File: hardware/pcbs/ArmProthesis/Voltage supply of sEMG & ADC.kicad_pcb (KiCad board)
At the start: 4 copper layers, 50.2 x 51.8 mm, 64 parts, among them Q1 BC817, Q2 BC817, Q3 BC817, U1 LT3045xMSE, U2 TPS7A4701RGWR, U3 LT8471EFE_TRPBF, U4 LT3094xMSE

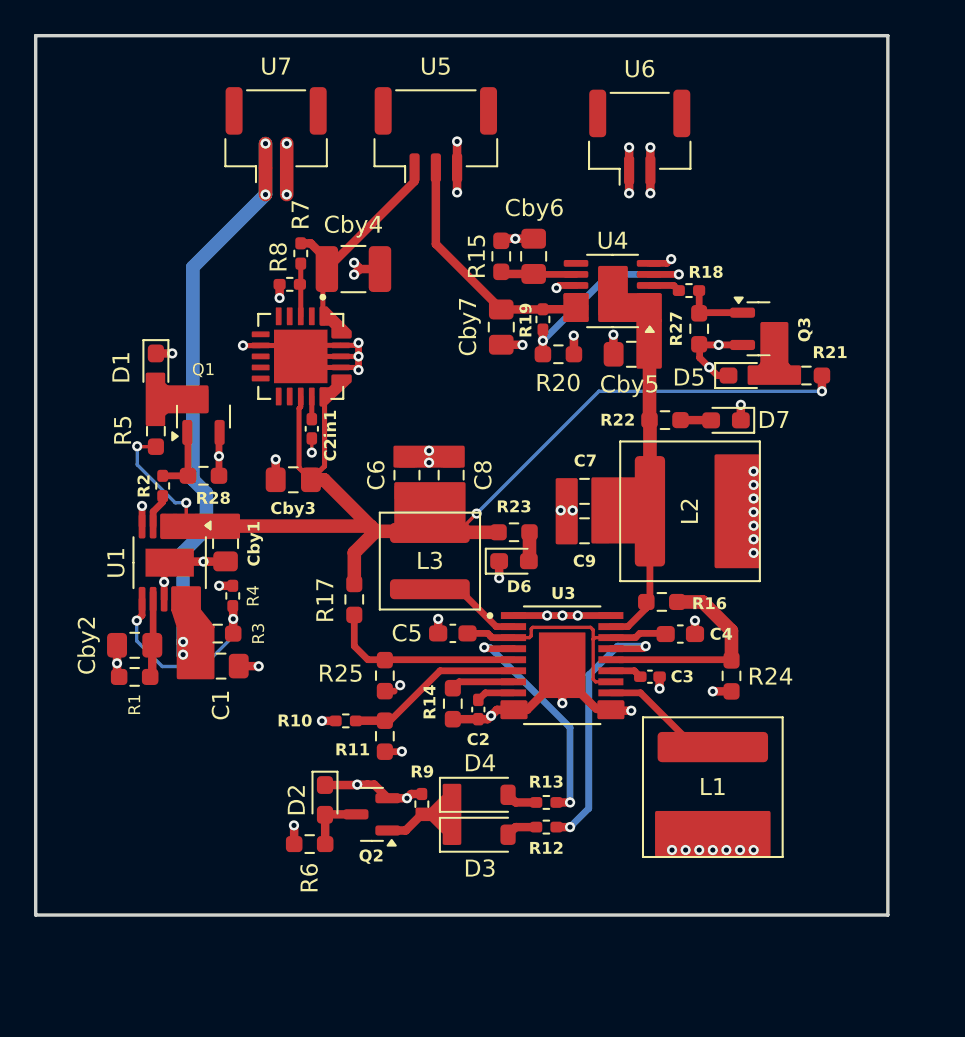
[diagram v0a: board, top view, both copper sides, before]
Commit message: Fixes
sEMG - minor
Voltage supply... - major but not fixed
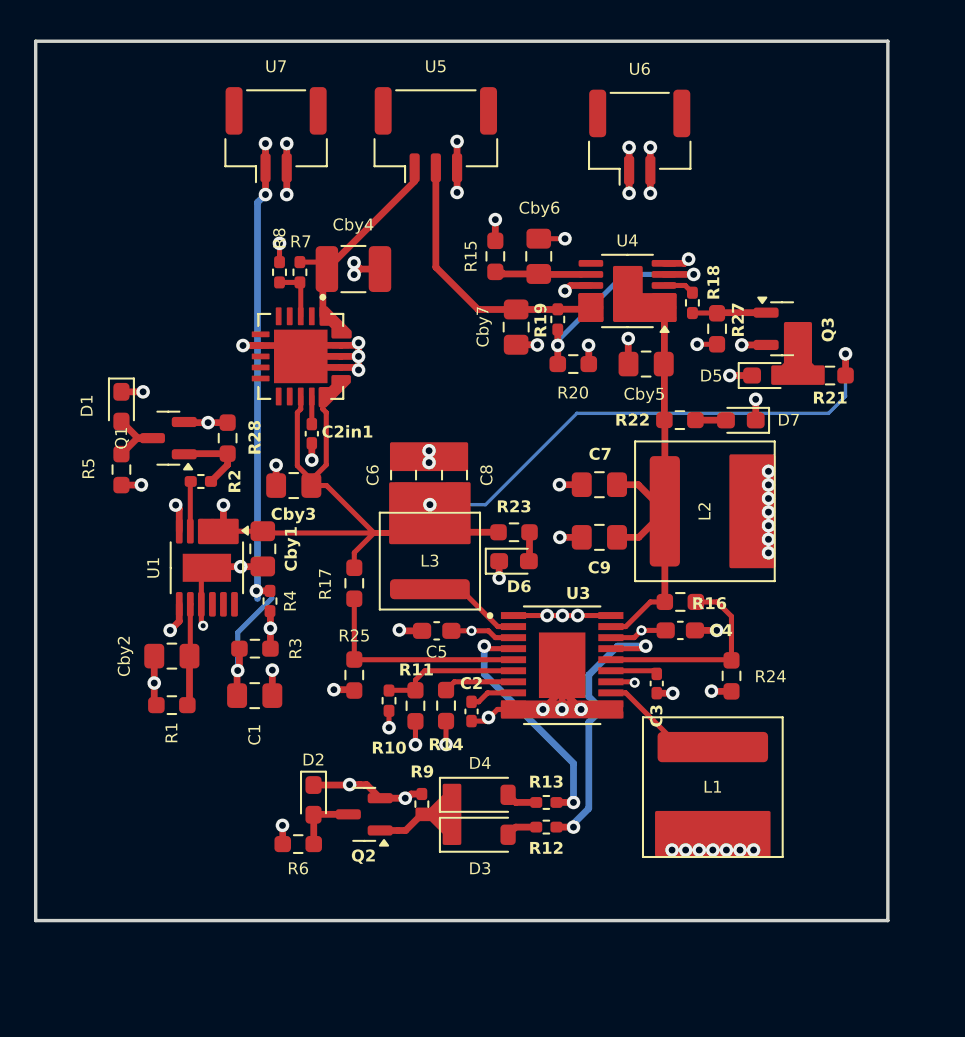
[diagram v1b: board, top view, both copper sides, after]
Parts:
- moved D1 3.04 mm to (99.2, 64.2)
- moved R5 3.04 mm to (99.2, 67.9)
- moved R10 2.81 mm to (114.9, 81.5), turned to -90 degrees
- moved R1 2.75 mm to (102.2, 81.8)
- moved C1 2.63 mm to (107.0, 81.2)
- moved R28 2.63 mm to (105.4, 66.1), turned to 90 degrees
- moved R11 2.54 mm to (116.5, 81.8)
- moved Q1 2.43 mm to (102.0, 66.1), turned to 180 degrees
- moved R3 2.36 mm to (107.1, 78.5)
- moved Cby2 2.28 mm to (102.2, 78.9)
- moved R2 2.26 mm to (103.9, 68.6), turned to 0 degrees
- moved Cby1 2.21 mm to (107.5, 72.6)
- moved R4 2.21 mm to (107.9, 75.6)
- moved U1 2.21 mm to (104.2, 73.7)
- moved R25 1.80 mm to (112.9, 80.0)
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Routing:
- net /+11.1V: track 112.7 -> 10.5 mm
- net GND: track 86.1 -> 99.0 mm, vias 55 -> 59
- net -6V: track 17.5 -> 27.3 mm
- net Net-(U3-SHOUT): track 16.6 -> 23.0 mm, vias 0 -> 3
- net +6V: track 67.9 -> 74.2 mm
- net Net-(D1-A): track 0.00 -> 4.44 mm
- net /+5V: track 37.7 -> 34.9 mm, vias 4 -> 3
- net Net-(U3-OV/UV): track 10.5 -> 8.29 mm
- net Net-(U1-SET): track 4.33 -> 6.06 mm
- net /-5.5V: track 14.1 -> 15.8 mm
- net Net-(U1-PGFB): track 12.0 -> 10.5 mm
- net Net-(U3-FB1): track 11.5 -> 13.0 mm
- net Net-(U1-PG): track 2.00 -> 2.94 mm
- net Net-(U3-SS2): track 1.88 -> 2.78 mm
- net Net-(U3-FB2): track 12.2 -> 11.7 mm
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- added copper zone on In2.Cu, net /+11.1V
- added copper zone on F.Cu, net GND

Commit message: Additional to last push
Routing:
- net GND: vias 59 -> 58
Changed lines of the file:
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@@
-	)
-	(via
-		(at 117.3 67.5)
-		(size 0.8)
-		(drill 0.4)
-		(layers "F.Cu" "B.Cu")
-		(net 1)
 	)
 	(via
@@
 	)
 	(via
-		(at 117.3 66.8)
+		(at 117.3 67.15)
 		(size 0.8)
 		(drill 0.4)
@@
 	)
 	(segment
-		(start 101.6675 68.3575)
-		(end 98.5 68.3575)
-		(width 0.4)
+		(start 100.37125 68.810385)
+		(end 104.010385 68.810385)
+		(width 0.3)
 		(layer "In2.Cu")
 		(net 8)
 	)
 	(segment
-		(start 103.01 69.7)
-		(end 101.6675 68.3575)
-		(width 0.4)
+		(start 104.010385 68.810385)
+		(end 105.2 70)
+		(width 0.3)
 		(layer "In2.Cu")
 		(net 8)

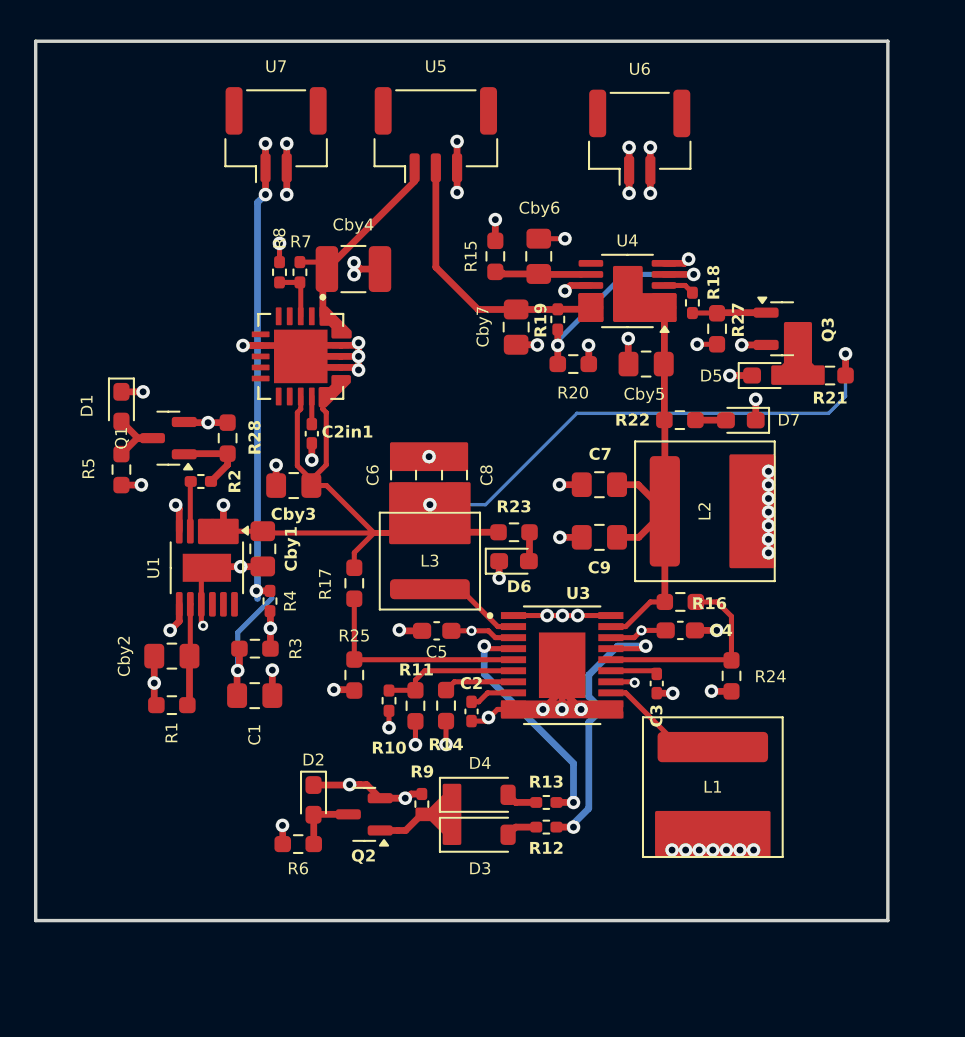
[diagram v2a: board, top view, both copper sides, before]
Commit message: Voltage supply sEMG & ADC v0.2
Major fixes. Mounting holes missing
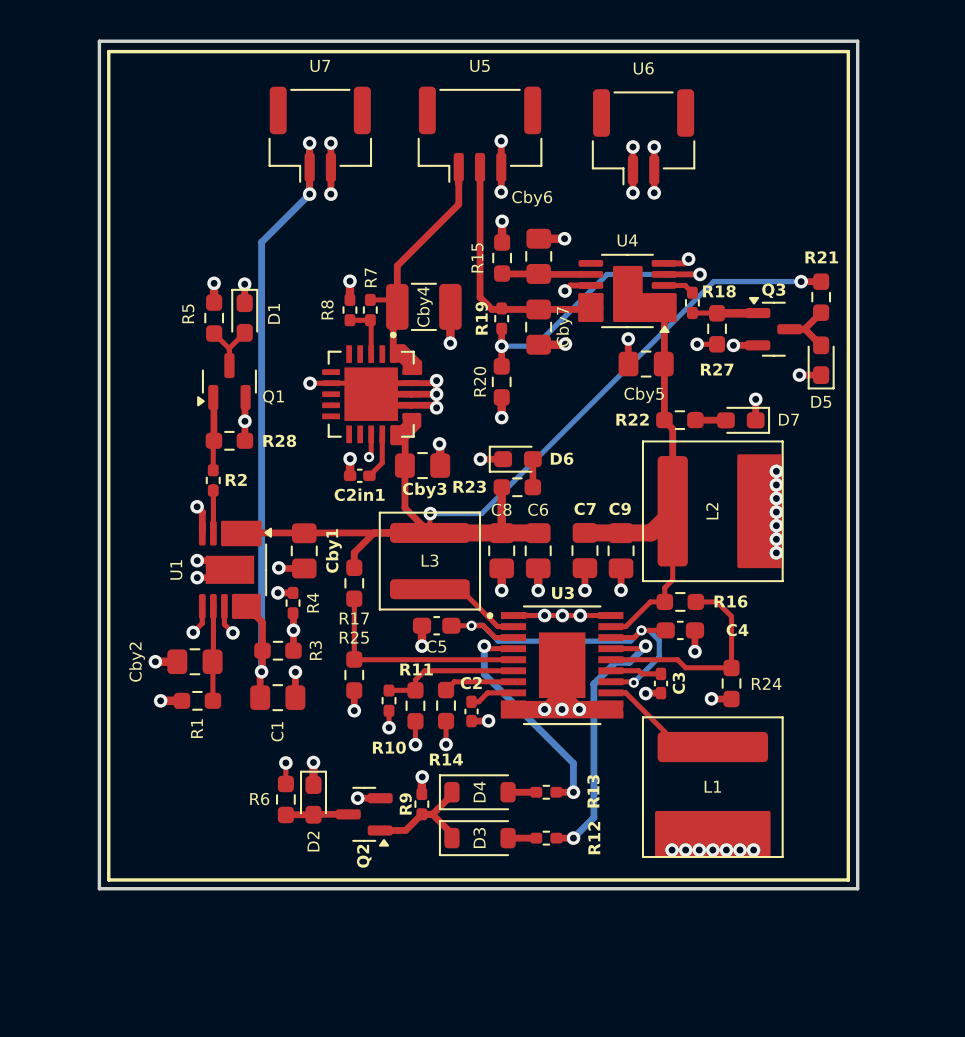
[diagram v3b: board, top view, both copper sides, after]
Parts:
- moved R5 10.5 mm to (104.7, 59.0), turned to 90 degrees
- moved C6 9.09 mm to (123.7, 72.7), turned to -90 degrees
- moved D1 8.94 mm to (106.5, 59.0)
- moved Cby3 7.67 mm to (116.9, 67.7), turned to 0 degrees
- moved D6 6.00 mm to (122.5, 67.3)
- moved C8 5.24 mm to (121.6, 72.7), turned to -90 degrees
- moved Q1 4.90 mm to (105.6, 62.7), turned to 90 degrees
- moved Cby4 4.70 mm to (117.0, 58.3)
- moved R7 4.70 mm to (113.8, 58.5)
- moved R8 4.70 mm to (112.6, 58.5)
- moved U2 4.70 mm to (113.9, 63.5)
- moved R21 4.64 mm to (140.4, 57.8), turned to 90 degrees
- moved R20 4.34 mm to (121.6, 62.8), turned to -90 degrees
- moved C7 3.97 mm to (126.5, 72.7), turned to 90 degrees
- moved C2in1 3.75 mm to (113.2, 68.3), turned to 180 degrees
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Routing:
- net +6V: track 74.5 -> 94.6 mm
- net GND: track 99.0 -> 91.7 mm, vias 58 -> 62
- net /+5V: track 34.9 -> 41.1 mm
- net Net-(D5-A): track 0.02 -> 4.52 mm
- net Net-(U4-PGFB): track 13.4 -> 17.4 mm
- net /+5.5V: track 14.2 -> 16.8 mm
- net Net-(D3-K): track 9.72 -> 7.69 mm
- net /-5.5V: track 15.8 -> 14.5 mm
- net Net-(U3-FB2): track 11.7 -> 12.8 mm
- net Net-(U2-NR): track 1.62 -> 2.75 mm
- net Net-(U3-SHOUT): track 23.0 -> 23.9 mm
- net Net-(Q3-B): track 4.36 -> 3.58 mm
- net -6V: track 27.3 -> 26.5 mm
- net Net-(D1-A): track 4.44 -> 3.76 mm
- net Net-(U1-SET): track 6.06 -> 5.44 mm
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- removed copper zone on F.Cu, net GND
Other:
- board size 50.2 x 51.8 mm -> 44.6 x 49.9 mm

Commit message: BMS v0.2v + polishment of Vsupply  board
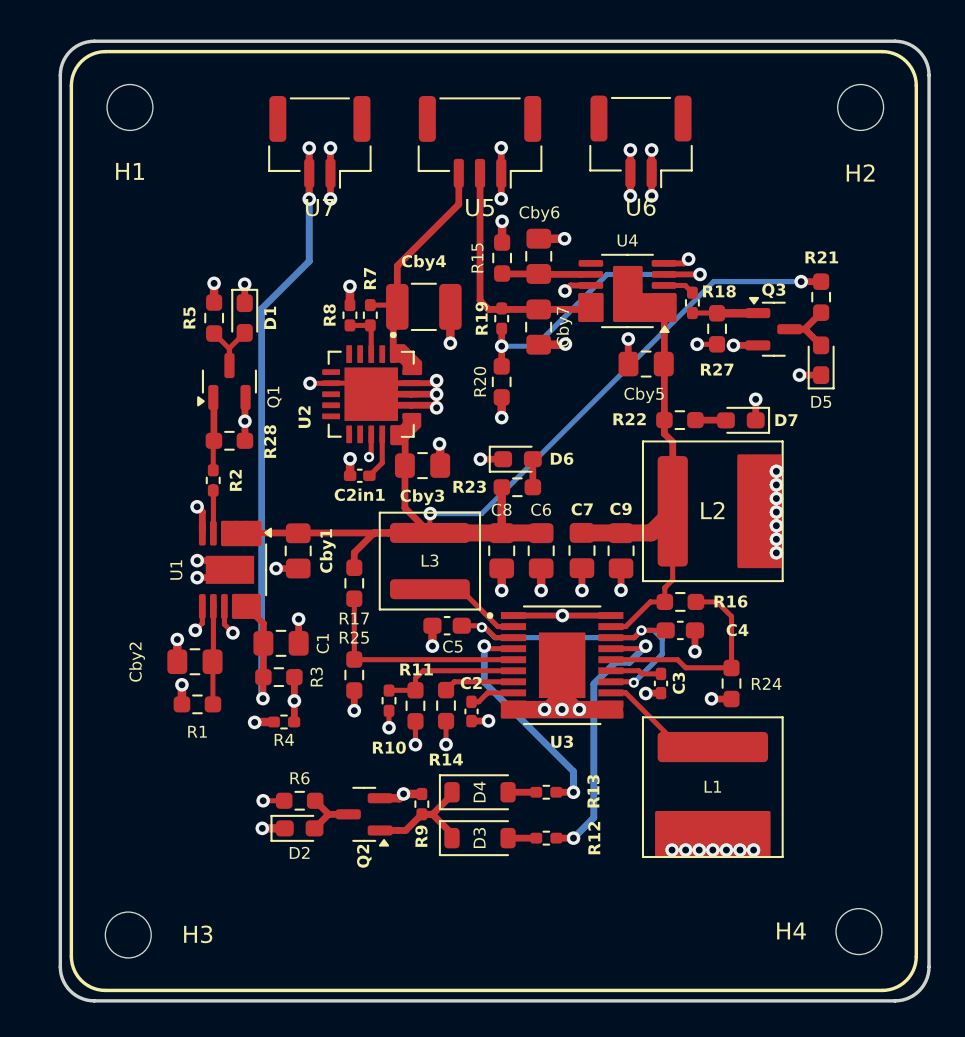
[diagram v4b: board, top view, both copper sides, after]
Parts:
- added H1: MountingHole, MountingHole:MountingHole_2.7mm_M2.5_DIN965, F.Cu at (99.7, 46.6)
- added H2: MountingHole, MountingHole:MountingHole_2.7mm_M2.5_DIN965, F.Cu at (142.7, 46.6)
- added H3: MountingHole, MountingHole:MountingHole_2.7mm_M2.5_DIN965, F.Cu at (99.6, 95.3)
- added H4: MountingHole, MountingHole:MountingHole_2.7mm_M2.5_DIN965, F.Cu at (142.6, 95.1)
- U5: footprint Connector_JST:JST_GH_BM03B-GHS-TBT_1x03-1MP_P1.25mm_Vertical -> Connector_JST:JST_GH_SM03B-GHS-TB_1x03-1MP_P1.25mm_Horizontal
- U6, U7: footprint Connector_JST:JST_GH_BM02B-GHS-TBT_1x02-1MP_P1.25mm_Vertical -> Connector_JST:JST_GH_SM02B-GHS-TB_1x02-1MP_P1.25mm_Horizontal
- moved R4 7.02 mm to (108.8, 82.8), turned to 0 degrees
- moved C1 3.20 mm to (108.6, 78.1)
- moved D2 1.86 mm to (109.7, 89.0), turned to 0 degrees
- moved R3 1.56 mm to (108.5, 80.1)
- moved R6 0.82 mm to (109.7, 87.4), turned to 180 degrees
- moved C5 0.61 mm to (118.4, 77.1)
- moved U7 0.45 mm to (110.9, 48.6), turned to 180 degrees
- moved U5 0.45 mm to (120.3, 48.6), turned to 180 degrees
- moved Cby1 0.36 mm to (109.6, 72.7)
- moved U6 0.31 mm to (129.8, 48.6), turned to 180 degrees
- moved R7 0.30 mm to (113.8, 58.8)
- moved R8 0.30 mm to (112.6, 58.8)
- moved R1 0.21 mm to (103.7, 81.7)
- moved C6 0.18 mm to (123.9, 72.7)
- moved C7 0.17 mm to (126.3, 72.7)
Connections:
- U5 pad 1: /+5.5V -> GND
- U5 pad 3: GND -> /+5.5V
- U7 pad 1: /+5V -> GND
- U7 pad 2: GND -> /+5V
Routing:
- net Net-(U1-PGFB): track 10.2 -> 12.2 mm
- net /+5V: track 41.1 -> 42.4 mm
- net Net-(U3-SHOUT): track 23.9 -> 22.7 mm
- net /+5.5V: track 16.8 -> 15.9 mm
- net GND: track 91.7 -> 91.9 mm, vias 62 -> 61
- net /+11.1V: vias 14 -> 12
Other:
- board size 44.6 x 49.9 mm -> 51.1 x 56.5 mm

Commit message: BMS v0.3 + main folder reconstruction
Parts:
- added G***: LOGO, LOGO, B.Cu at (105.4, 89.1)
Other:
- board text added: "SL-sEMG/ADC-PSU v0.3"

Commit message: Cosmetics xd
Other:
- board text added: "SL-sEMG&ADC-PSU v0.3"
- board text removed: "SL-sEMG/ADC-PSU v0.3"
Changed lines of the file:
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@@
 		(tags "connector JST GH horizontal")
 		(property "Reference" "U7"
-			(at 0 -3.9 180)
+			(at 0.025 -4.55 180)
 			(layer "F.SilkS")
 			(effects
@@
 		(tags "capacitor handsolder")
 		(property "Reference" "Cby7"
-			(at -0.025 -1.45 90)
+			(at 2.45 -0.025 180)
 			(layer "F.SilkS")
 			(effects
@@
 		(tags "connector JST GH horizontal")
 		(property "Reference" "U6"
-			(at 0 -3.9 180)
+			(at 0.025 -4.35 180)
 			(layer "F.SilkS")
 			(effects
@@
 		(tags "capacitor handsolder")
 		(property "Reference" "Cby2"
-			(at 3.465 0 90)
+			(at 2.6725 0.02 90)
 			(layer "F.SilkS")
 			(effects
@@
 		(tags "capacitor handsolder")
 		(property "Reference" "C4"
-			(at -3.3625 -0.009375 0)
+			(at -2.5625 0.025 0)
 			(layer "F.SilkS")
 			(effects
@@
 		(tags "connector JST GH horizontal")
 		(property "Reference" "U5"
-			(at 0 -3.9 180)
+			(at 0.175 0 180)
 			(layer "F.SilkS")
 			(effects
@@
 		)
 	)
-	(gr_text "SL-sEMG/ADC-PSU v0.3"
-		(at 132.85 46.85 0)
+	(gr_text "SL-sEMG&ADC-PSU v0.3"
+		(at 135.35 46.6 0)
 		(layer "B.SilkS")
 		(effects

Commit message: Vs of sEMG and ADC v0.4
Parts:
- moved R24 5.22 mm to (136.8, 75.6), turned to 0 degrees
- moved C7 3.31 mm to (127.5, 69.6), turned to 0 degrees
- moved R25 2.80 mm to (112.9, 77.2)
- moved R17 2.00 mm to (112.9, 72.6)
- moved C9 1.32 mm to (127.5, 71.9), turned to 0 degrees
- moved L1 1.24 mm to (134.0, 85.4)
- moved C3 1.07 mm to (131.9, 80.0), turned to 0 degrees
- moved U4 0.83 mm to (129.8, 57.3)
- moved D5 0.83 mm to (141.2, 61.4)
- moved R18 0.83 mm to (133.6, 58.0)
- moved R21 0.83 mm to (141.2, 57.7)
- moved R27 0.83 mm to (135.1, 59.5)
- moved Q3 0.83 mm to (138.4, 59.6)
- moved Cby5 0.51 mm to (130.6, 61.6)
- moved D7 0.51 mm to (136.2, 64.9)
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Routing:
- net -6V: track 26.7 -> 4.29 mm
- net +6V: track 95.0 -> 72.8 mm
- net GND: track 91.9 -> 85.2 mm, vias 61 -> 60
- net Net-(U4-PGFB): track 17.4 -> 18.6 mm
- net Net-(U4-SET): track 4.67 -> 5.80 mm
- net Net-(U3-SHOUT): track 22.7 -> 23.8 mm
- net Net-(U3-FB2): track 12.8 -> 12.1 mm
- net /-5.5V: track 14.3 -> 14.8 mm
- net Net-(U3-PG2): track 16.7 -> 17.2 mm
- net Net-(U3-C3): track 7.32 -> 6.81 mm
- net /+11.1V: vias 12 -> 13
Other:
- board text added: "SL-sEMG&ADC-PSU v0.4"
- board text removed: "SL-sEMG&ADC-PSU v0.3"
